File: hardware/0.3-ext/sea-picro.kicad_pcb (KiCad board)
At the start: 4 copper layers, 17.8 x 33 mm, 59 parts, among them J1 USB_C_Receptacle_USB2.0, J2 0.1" x 12, J3 0.1" x 12, J4 D+, J5 D-, J6 0.1" x 5, J7 2.54, Q1 2N7002VC-7, Q2 2N7002VC-7, U1 AP7365-33WG-7, U2 GD25Q64CWIGR, U3 RP2040, U4 74LVC1T45Z6-7, Y1 12MHz

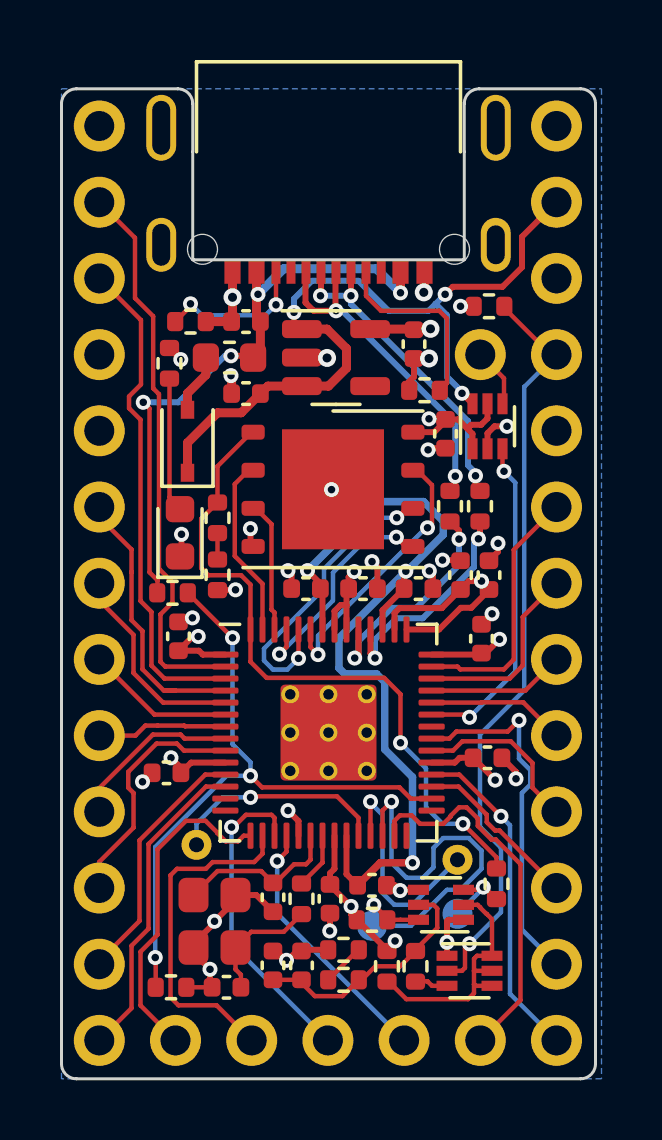
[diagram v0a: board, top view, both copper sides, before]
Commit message: sea picro footprint overhaul
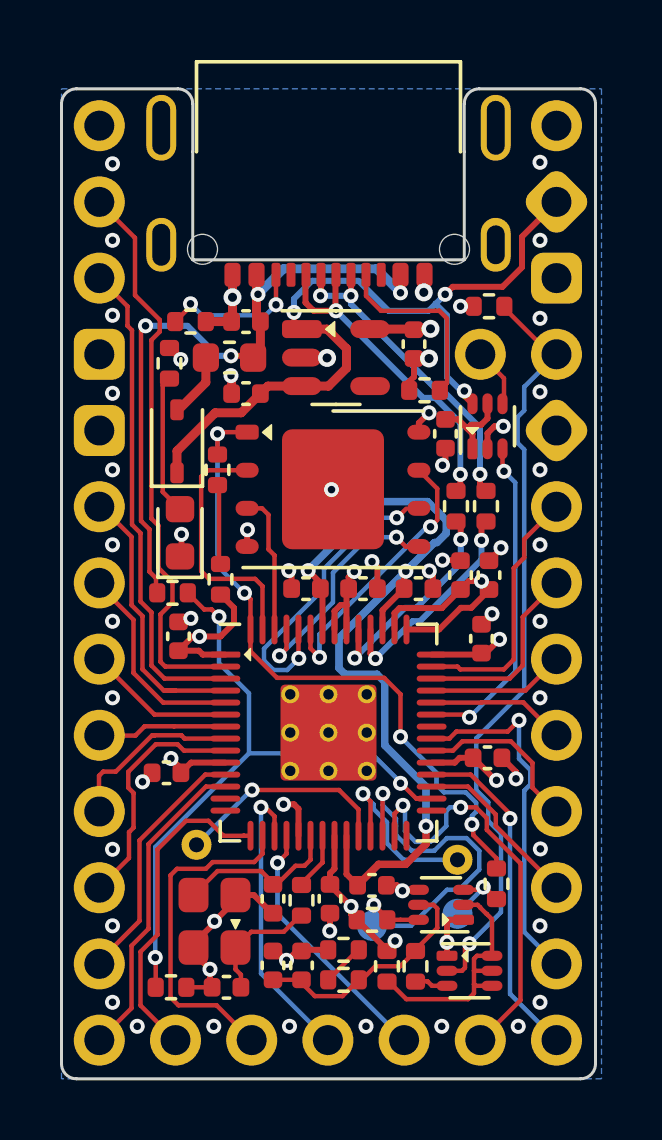
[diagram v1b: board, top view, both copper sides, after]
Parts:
- removed J3: 0.1" x 12, josh-connectors:Castellated_Short_P2.54x12
- removed J4: D+, josh-connectors:PinHeader_1x01_P2.54mm_Circle
- removed J5: D-, josh-connectors:PinHeader_1x01_P2.54mm_Circle
- removed J6: 0.1" x 5, josh-connectors:PinHeader_1x05_P2.54mm_Circle
- removed J7: 2.54, josh-connectors:PinHeader_1x01_P2.54mm_Circle
- D1: footprint Diode_SMD:D_SOD-323 -> josh-passives-smt:D_SOD-323
- J2: value 0.1" x 12 -> Sea-Picro; footprint josh-connectors:Castellated_Short_P2.54x12 -> josh-module:Sea-Picro_EXT_Pins
- Q1, Q2, U4: footprint Package_TO_SOT_SMD:SOT-563 -> josh-soic-sot-etc:SOT-563
- U1: footprint Package_TO_SOT_SMD:SOT-23-5 -> josh-soic-sot-etc:SOT-23-5
- U2: footprint Package_SON:WSON-8-1EP_6x5mm_P1.27mm_EP3.4x4mm -> josh-dfn-qfn:WSON-8-1EP_6x5mm_P1.27mm_EP3.4x4mm
- moved J2 17.0 mm to (126.1, 91.3), turned to 0 degrees
- moved R10 1.60 mm to (122.5, 87.5)
- moved D1 0.35 mm to (121.2, 86.5)
- moved R7 0.20 mm to (130.4, 88.7)
- moved R8 0.20 mm to (131.4, 88.7)
- moved R6 0.18 mm to (122.6, 91.2)
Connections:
- J2 pad 1: /9 -> /USB+
- J2 pad 10: GND -> /6
- J2 pad 11: /1_RX0 -> /7
- J2 pad 12: /0_TX0 -> /8
- J2 pad 2: /8 -> /0_TX0
- J2 pad 3: /7 -> /1_RX0
- J2 pad 4: /6 -> GND
- J2 pad 5: /5 -> GND
- J2 pad 6: /4 -> /2_SDA1
- J2 pad 8: /2_SDA1 -> /4
- J2 pad 9: GND -> /5
- U4 pad 4: Net-(J7-Pad1) -> /LED_5V
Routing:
- net /FLASH_SD1: track 6.03 -> 8.46 mm
- net VBUS: track 20.0 -> 22.4 mm
- net Net-(J7-Pad1): track 1.97 -> 0.00 mm
- net /LED_5V: track 0.00 -> 1.97 mm
- net Net-(R10-Pad1): track 0.88 -> 2.65 mm
- net /16: track 12.5 -> 14.2 mm, vias 0 -> 2
- net /SWDIO: track 7.63 -> 6.06 mm
- net /nRST: track 15.1 -> 13.7 mm
- net /14: track 10.7 -> 9.92 mm
- net /D+: track 8.03 -> 7.31 mm
- net +3V3: track 34.1 -> 34.8 mm, vias 13 -> 12
- net GND: track 28.3 -> 28.4 mm, vias 26 -> 54
- net /FLASH_nCS: vias 2 -> 4

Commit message: rst moved to new footprints, clean up ext
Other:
- board text removed: "G"
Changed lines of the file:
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@@
     (effects (font (size 1 1) (thickness 0.15)) (justify mirror))
   )
-  (gr_text "G" (at 132.4 81.6) (layer "B.SilkS")
+  (gr_text "GND" (at 131.35 81.675) (layer "B.SilkS")
     (effects (font (size 1 1) (thickness 0.15)) (justify mirror))
   )
@@
   (segment (start 121.09 94.86) (end 120.86 94.86) (width 0.15) (layer "F.Cu") (net 22))
   (segment (start 119.634511 89.734511) (end 118.64 88.74) (width 0.15) (layer "F.Cu") (net 22))
-  (segment (start 118.56 81.11) (end 119.5 82.05) (width 0.15) (layer "F.Cu") (net 23))
-  (segment (start 120.299021 94.024021) (end 120.735002 94.46) (width 0.15) (layer "F.Cu") (net 23))
+  (segment (start 119.934021 91.886877) (end 120.299021 92.251877) (width 0.15) (layer "F.Cu") (net 23))
+  (segment (start 119.934022 89.61045) (end 119.934021 91.886877) (width 0.15) (layer "F.Cu") (net 23))
+  (segment (start 119.65048 82.85048) (end 119.65048 89.326908) (width 0.15) (layer "F.Cu") (net 23))
+  (segment (start 119.5 82.05) (end 119.5 82.7) (width 0.15) (layer "F.Cu") (net 23))
+  (segment (start 120.299021 92.251877) (end 120.299021 94.024021) (width 0.15) (layer "F.Cu") (net 23))
   (segment (start 119.5 82.7) (end 119.65048 82.85048) (width 0.15) (layer "F.Cu") (net 23))
   (segment (start 119.65048 89.326908) (end 119.934022 89.61045) (width 0.15) (layer "F.Cu") (net 23))
-  (segment (start 119.5 82.05) (end 119.5 82.7) (width 0.15) (layer "F.Cu") (net 23))
-  (segment (start 119.65048 82.85048) (end 119.65048 89.326908) (width 0.15) (layer "F.Cu") (net 23))
   (segment (start 120.735002 94.46) (end 122.7625 94.46) (width 0.15) (layer "F.Cu") (net 23))
-  (segment (start 119.934022 89.61045) (end 119.934021 91.886877) (width 0.15) (layer "F.Cu") (net 23))
-  (segment (start 119.934021 91.886877) (end 120.299021 92.251877) (width 0.15) (layer "F.Cu") (net 23))
-  (segment (start 120.299021 92.251877) (end 120.299021 94.024021) (width 0.15) (layer "F.Cu") (net 23))
+  (segment (start 120.299021 94.024021) (end 120.735002 94.46) (width 0.15) (layer "F.Cu") (net 23))
+  (segment (start 118.56 81.11) (end 119.5 82.05) (width 0.15) (layer "F.Cu") (net 23))
   (segment (start 120.296984 89.126268) (end 120.296984 83.174354) (width 0.15) (layer "F.Cu") (net 24))
   (segment (start 119.75 81.678368) (end 119.75 79.77) (width 0.15) (layer "F.Cu") (net 24))
